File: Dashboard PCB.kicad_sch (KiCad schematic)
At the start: 36 parts, among them J1 Controls_Leader_Export_02x06, J2 Conn_02x03_CAN, J4 FAN_CTRL_01x02, J5 Horn_In_01x02, J6 Horn_Out_01x02, J7 Conn_02x03_CAN

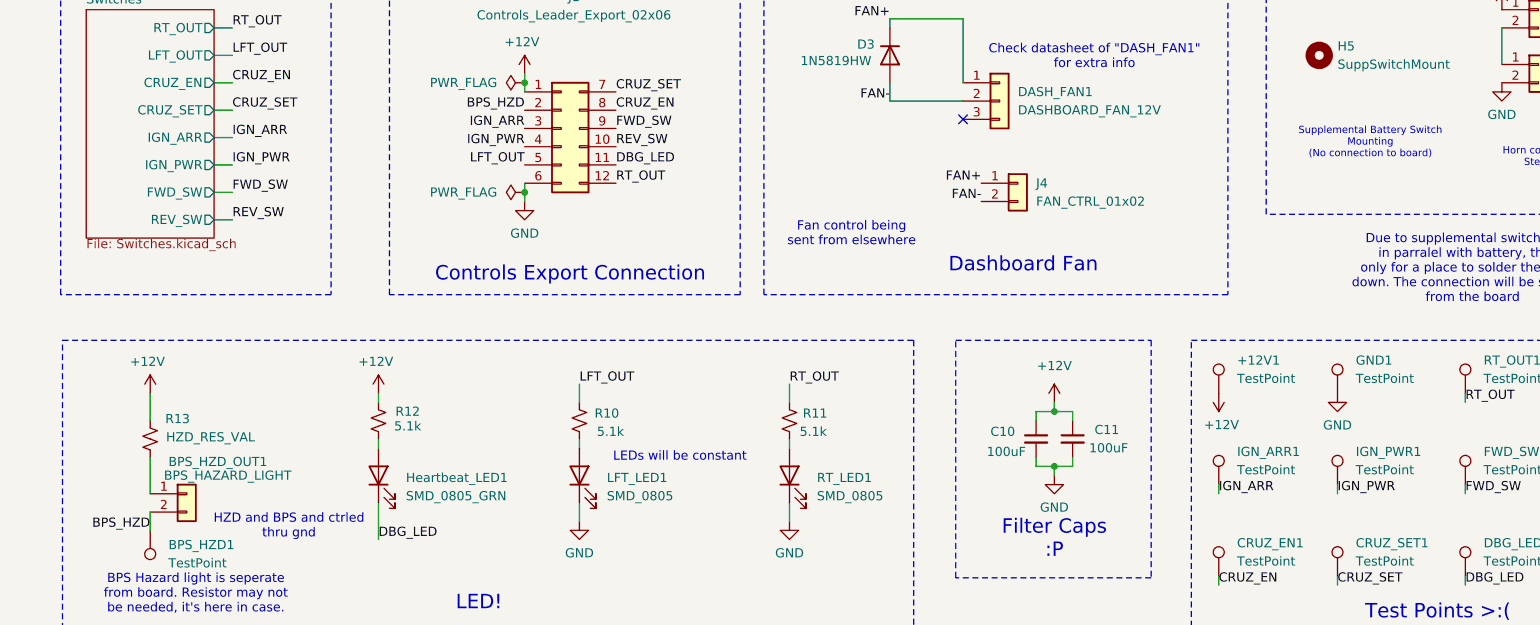
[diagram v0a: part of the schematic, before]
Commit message: Changed size and rerouted
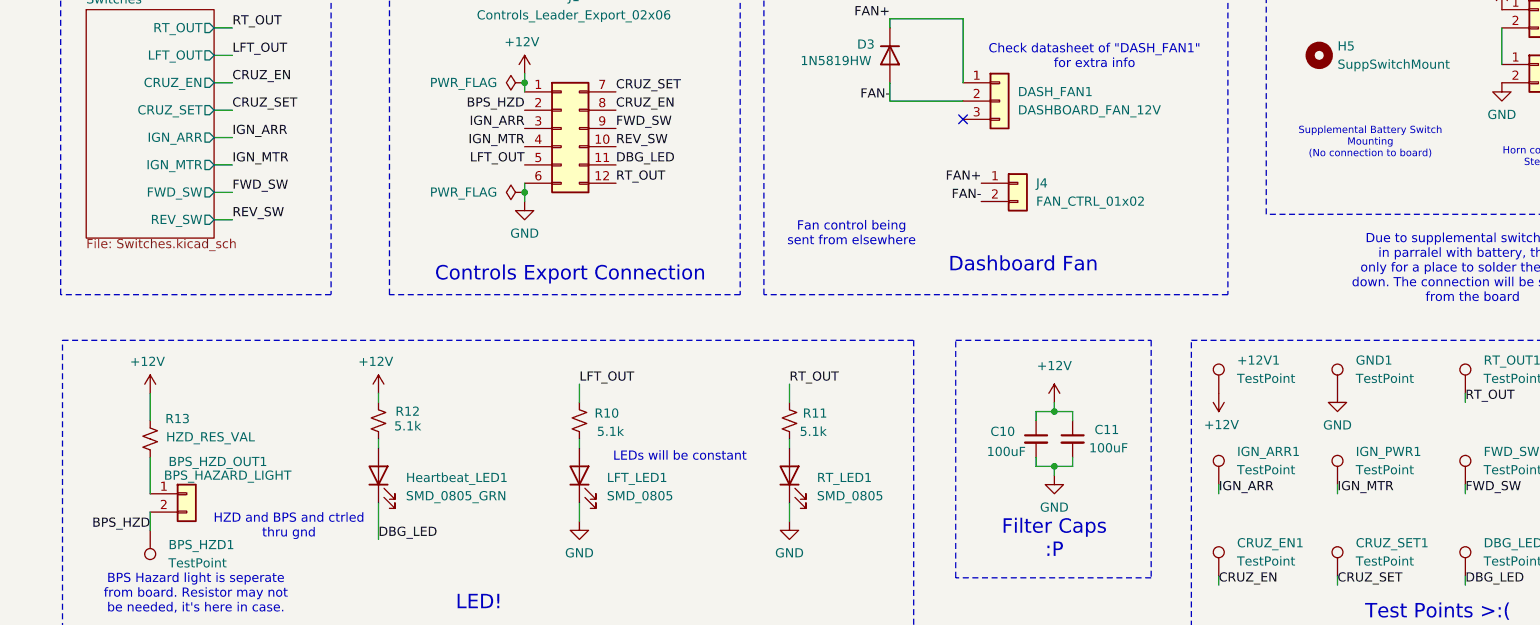
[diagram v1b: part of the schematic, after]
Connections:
- net IGN_PWR renamed IGN_MTR
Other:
- sheet Switches ports: added IGN_MTR; removed IGN_PWR
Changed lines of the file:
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@@
 		)
 	)
-	(label "IGN_PWR"
+	(label "IGN_MTR"
 		(at 95.25 87.63 180)
 		(fields_autoplaced yes)
@@
 		)
 	)
-	(label "IGN_PWR"
+	(label "IGN_MTR"
 		(at 54.61 90.17 0)
 		(fields_autoplaced yes)
@@
 		)
 	)
-	(label "IGN_PWR"
+	(label "IGN_MTR"
 		(at 208.28 135.89 0)
 		(fields_autoplaced yes)
@@
 			)
 		)
-		(pin "IGN_PWR" output
+		(pin "IGN_MTR" output
 			(at 52.07 90.17 0)
 			(effects

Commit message: A bunch of stuff
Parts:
- removed BPS_HZD_OUT1: BPS_HAZARD_LIGHT, Connector_Molex:Molex_Micro-Fit_3.0_43650-0215_1x02_P3.00mm_Vertical, symbol Connector_Generic:Conn_01x02
- added BPS_HZD_LED1: SMD_0805_RED, LED_SMD:LED_0805_2012Metric, symbol Device:LED
- added J8: Supp_Out, Connector_Molex:Molex_Micro-Fit_3.0_43650-0200_1x02_P3.00mm_Horizontal, symbol Connector_Generic:Conn_01x02
- added J9: Supp_In, Connector_Molex:Molex_Micro-Fit_3.0_43650-0215_1x02_P3.00mm_Vertical, symbol Connector_Generic:Conn_01x02
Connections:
- net BPS_HZD: now also BPS_HZD_LED1.1 (K)
- net at R13.2: now also BPS_HZD_LED1.2 (A)
- new net Supp+: J8.1 (Pin_1), J9.1 (Pin_1)
- new net Supp-: J8.2 (Pin_2), J9.2 (Pin_2)
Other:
- note removed: "BPS Hazard light is seperate from board. Resistor may not be needed, it's here in case."
- note removed: "HZD and BPS and ctrled thru gnd"
- note removed: "Supplemental Battery Switch Mounting (No connection to board)"
- moved on the sheet: H5

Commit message: Supp changes
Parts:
- added D4: LED, LED_SMD:LED_0805_2012Metric, symbol Device:LED
- added R14: 5.1k, Resistor_SMD:R_0805_2012Metric, symbol Device:R_Small_US
- J8: footprint Connector_Molex:Molex_Micro-Fit_3.0_43650-0200_1x02_P3.00mm_Horizontal -> Connector_Molex:Molex_Micro-Fit_3.0_43650-0300_1x03_P3.00mm_Horizontal; symbol Connector_Generic:Conn_01x02 -> Connector_Generic:Conn_01x03
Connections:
- net Supp-: now also J8.3 (Pin_3), D4.1 (K); no longer J8.2 (Pin_2), J9.2 (Pin_2)
- new net: D4.2 (A), R14.2
- new net LV_EN: J8.2 (Pin_2), J9.2 (Pin_2), R14.1
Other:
- moved on the sheet: H5, J9

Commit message: Final changes for now
added p/n n stuff
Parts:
- D3: P/N (none) -> 1N5819HW-7-F
- D4: P/N (none) -> APTD2012LCGCK
- DASH_FAN1, J8: P/N (none) -> 43650-0300
- J1: P/N (none) -> 43045-1200
- J2: P/N (none) -> 43045-0600
- J4, J5, J6: P/N (none) -> 43650-0200
- J7: P/N (none) -> 43045-0400
- J9: P/N (none) -> 43650-0215

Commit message: Uhh
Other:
- note added: "Might need to add mosfet between horn so there isnt a bunch of current going thru horn button"
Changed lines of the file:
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@@
+		)
+	)
+	(text "Might need to add mosfet between horn\nso there isnt a bunch of current going thru\nhorn button"
+		(exclude_from_sim no)
+		(at 279.146 77.216 0)
+		(effects
+			(font
+				(size 1.27 1.27)
+			)
 		)
 	)

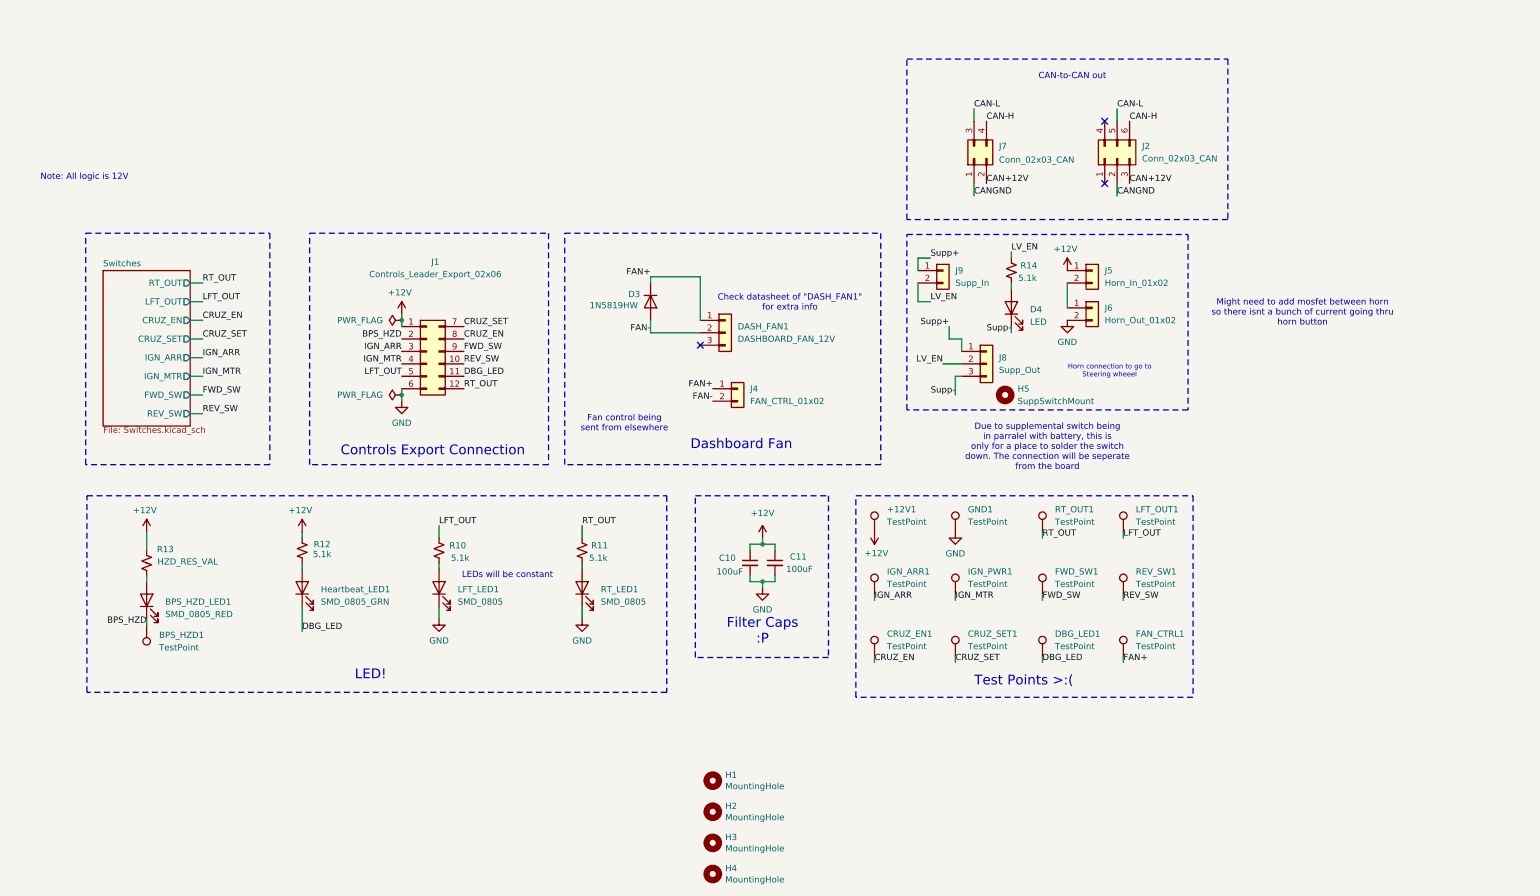
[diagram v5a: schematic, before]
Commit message: Delete submodule directory
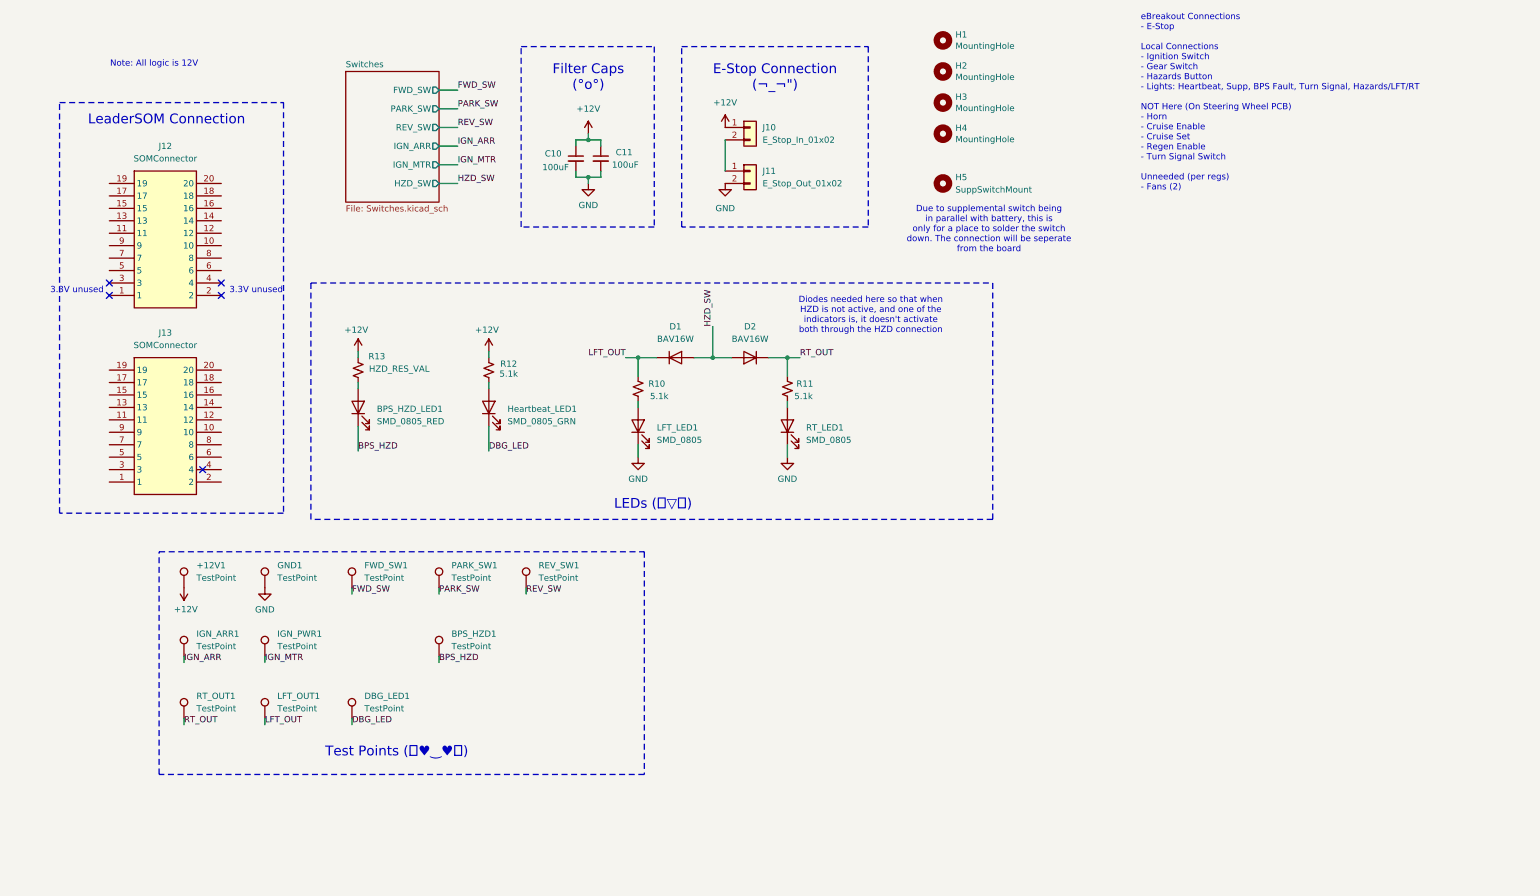
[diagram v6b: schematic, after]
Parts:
- removed CRUZ_EN1, CRUZ_SET1, FAN_CTRL1: TestPoint, TestPoint:TestPoint_Pad_1.0x1.0mm, symbol Connector:TestPoint
- removed D3: 1N5819HW, Diode_SMD:D_SOD-123, symbol Device:D
- removed D4: LED, LED_SMD:LED_0805_2012Metric, symbol Device:LED
- removed DASH_FAN1: DASHBOARD_FAN_12V, Connector_Molex:Molex_Micro-Fit_3.0_43650-0300_1x03_P3.00mm_Horizontal, symbol Connector_Generic:Conn_01x03
- removed J1: Controls_Leader_Export_02x06, Connector_Molex:Molex_Micro-Fit_3.0_43045-1200_2x06_P3.00mm_Horizontal, symbol Connector_Generic:Conn_02x06_Top_Bottom
- removed J2: Conn_02x03_CAN, Connector_Molex:Molex_Micro-Fit_3.0_43045-0600_2x03_P3.00mm_Horizontal, symbol Connector_Generic:Conn_02x03_Top_Bottom
- removed J4: FAN_CTRL_01x02, Connector_Molex:Molex_Micro-Fit_3.0_43650-0200_1x02_P3.00mm_Horizontal, symbol Connector_Generic:Conn_01x02
- removed J5: Horn_In_01x02, Connector_Molex:Molex_Micro-Fit_3.0_43650-0200_1x02_P3.00mm_Horizontal, symbol Connector_Generic:Conn_01x02
- removed J6: Horn_Out_01x02, Connector_Molex:Molex_Micro-Fit_3.0_43650-0200_1x02_P3.00mm_Horizontal, symbol Connector_Generic:Conn_01x02
- removed J7: Conn_02x03_CAN, Connector_Molex:Molex_Micro-Fit_3.0_43045-0400_2x02_P3.00mm_Horizontal, symbol Connector_Generic:Conn_02x02_Top_Bottom
- removed J8: Supp_Out, Connector_Molex:Molex_Micro-Fit_3.0_43650-0300_1x03_P3.00mm_Horizontal, symbol Connector_Generic:Conn_01x03
- removed J9: Supp_In, Connector_Molex:Molex_Micro-Fit_3.0_43650-0215_1x02_P3.00mm_Vertical, symbol Connector_Generic:Conn_01x02
- removed R14: 5.1k, Resistor_SMD:R_0805_2012Metric, symbol Device:R_Small_US
- added D1, D2: BAV16W, Diode_SMD:D_SOD-123, symbol Diode:BAV16W
- added J10: E_Stop_In_01x02, symbol Connector_Generic:Conn_01x02
- added J11: E_Stop_Out_01x02, symbol Connector_Generic:Conn_01x02
- added J12, J13: SOMConnector, UTSVT_Connectors:Molex_52465-2070, symbol connectors:SOMConnector
- added PARK_SW1: TestPoint, TestPoint:TestPoint_Pad_1.0x1.0mm, symbol Connector:TestPoint
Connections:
- net +12V: now also J10.1 (Pin_1)
- net GND: now also J11.2 (Pin_2)
- net LFT_OUT: now also D1.1 (K)
- net RT_OUT: now also D2.1 (K)
- new net: J10.2 (Pin_2), J11.1 (Pin_1)
- new net HZD_SW: D1.2 (A), D2.2 (A)
- new net PARK_SW: PARK_SW1.1
- no-connect marks 3 -> 5
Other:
- sheet Switches ports: added HZD_SW, PARK_SW; removed CRUZ_EN, CRUZ_SET, LFT_OUT, RT_OUT
- note added: "3.3V unused"
- note added: "Diodes needed here so that when HZD is not active, and one of the indicators is, it doesn't activate both through the HZD connection"
- note added: "Due to supplemental switch being in parallel with battery, this is only for a place to solder the switch down. The connection will be seperate from the board"
- note added: "E-Stop Connection (¬_¬")"
- note added: "Filter Caps (°o°)"
- note added: "LEDs (＾▽＾)"
- note added: "LeaderSOM Connection"
- note added: "Test Points (｡♥‿♥｡)"
- note added: "eBreakout Connections - E-Stop Local Connections - Ignition Switch - Gear Switch - Hazards Button - Lights: Heartbeat, Supp, BPS Fault, Turn Signal, Hazards/LFT/RT NOT Here (On Steering Wheel PCB) - Horn - Cruise Enable - Cruise Set - Regen Enable - Turn Signal Switch Unneeded (per regs) - Fans (2)"
- note removed: "CAN-to-CAN out"
- note removed: "Check datasheet of "DASH_FAN1" for extra info"
- note removed: "Controls Export Connection"
- note removed: "Dashboard Fan"
- note removed: "Due to supplemental switch being in parralel with battery, this is only for a place to solder the switch down. The connection will be seperate from the board"
- note removed: "Fan control being sent from elsewhere"
- note removed: "Filter Caps :P"
- note removed: "Horn connection to go to Steering wheeel"
- note removed: "LED!"
- note removed: "LEDs will be constant"
- note removed: "Might need to add mosfet between horn so there isnt a bunch of current going thru horn button"
- note removed: "Test Points >:("
- moved on the sheet: +12V1, BPS_HZD1, BPS_HZD_LED1, C10, C11, DBG_LED1, FWD_SW1, GND1, H1, H2, H3, H4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

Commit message: Schematic updates. Ready for review, I think.
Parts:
- removed J10: E_Stop_In_01x02, symbol Connector_Generic:Conn_01x02
- removed J11: E_Stop_Out_01x02, symbol Connector_Generic:Conn_01x02
- removed J12, J13: SOMConnector, UTSVT_Connectors:Molex_52465-2070, symbol connectors:SOMConnector
- added J1: ~, symbol connectors:LSOM_DaughterConn
- added J4: CarCAN_ConnIn_01x02, Connector_Molex:Molex_Micro-Fit_3.0_43650-0215_1x02_P3.00mm_Vertical, symbol Connector_Generic:Conn_01x02
- added J5: InternalCAN_ConnIn_01x02, Connector_Molex:Molex_Micro-Fit_3.0_43650-0215_1x02_P3.00mm_Vertical, symbol Connector_Generic:Conn_01x02
- added J6: InternalCAN_ConnOut_01x02, Connector_Molex:Molex_Micro-Fit_3.0_43650-0215_1x02_P3.00mm_Vertical, symbol Connector_Generic:Conn_01x02
- added J7: E_Stop_In_01x02, Connector_Molex:Molex_Micro-Fit_3.0_43650-0215_1x02_P3.00mm_Vertical, symbol Connector_Generic:Conn_01x02
- added J8: CarCAN_ConnOut_01x02, Connector_Molex:Molex_Micro-Fit_3.0_43650-0215_1x02_P3.00mm_Vertical, symbol Connector_Generic:Conn_01x02
- added J9: E_Stop_Out_01x02, Connector_Molex:Molex_Micro-Fit_3.0_43650-0215_1x02_P3.00mm_Vertical, symbol Connector_Generic:Conn_01x02
- BPS_HZD_LED1: P/N APTD2012LCGCK -> APTD2012LSURCK
- C10, C11: value 100uF -> 10uF; P/N C0805C103J5RACTU -> C0805C106M3PAC7210
- R10, R11, R12: value 5.1k -> 470; P/N CRCW0805100RFKEAHP -> CRCW0805470RFKEAC
- R13: value HZD_RES_VAL -> 470; P/N CRCW0805100RFKEAHP -> CRCW0805470RFKEAC
- renumbered +12V1 to +12V
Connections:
- net +12V: now also J1.21 (12VExt), J1.22 (12VExt), J1.23 (12VExt), J1.24 (12VExt), J7.1 (Pin_1); no longer R12.1, R13.1
- net FWD_SW: now also J1.20 (SPI2_SCK)
- net GND: now also BPS_HZD_LED1.1 (K), Heartbeat_LED1.1 (K), J1.10 (GND), J1.12 (GND), J1.13 (GND), J1.15 (GND), J1.25 (GND), J1.26 (GND), J1.27 (GND), J1.28 (GND), J1.29 (GND), J1.38 (GND), J1.40 (GND), J9.2 (Pin_2)
- net IGN_ARR: now also J1.44 (ADC1_IN3)
- net IGN_MTR: now also J1.42 (ADC1_IN2)
- net LFT_OUT: now also R11.1, J1.11 (I2C3_SCL); no longer R10.1
- net PARK_SW: now also J1.18 (SPI2_MOSI)
- net REV_SW: now also J1.16 (SPI2_CS)
- net RT_OUT: now also R12.1, J1.9 (I2C3_SDA); no longer R11.1
- net at RT_LED1.2 (A): now also R12.2; no longer R11.2
- net at Heartbeat_LED1.2 (A): now also R10.2; no longer R12.2
- net at LFT_LED1.2 (A): now also R11.2; no longer R10.2
- net BPS_HZD renamed BPS_HZD_OUT
- net BPS_HZD_OUT: now also R13.1, J1.19 (UART5_RX); no longer BPS_HZD_LED1.1 (K)
- net DBG_LED renamed DBG_LED_OUT
- net DBG_LED_OUT: now also R10.1, J1.17 (UART5_TX); no longer Heartbeat_LED1.1 (K)
- new net: J7.2 (Pin_2), J9.1 (Pin_1)
- new net +3.3V: J1.1 (+3.3V), J1.2 (+3.3V), J1.3 (+3.3V), J1.4 (+3.3V), J1.45 (+3.3V), J1.46 (+3.3V), J1.47 (+3.3V), J1.48 (+3.3V)
- new net CCAN_H: J1.30 (CCAN_H), J4.2 (Pin_2), J8.2 (Pin_2)
- new net CCAN_L: J1.32 (CCAN_L), J4.1 (Pin_1), J8.1 (Pin_1)
- new net ICAN_H: J1.6 (ICAN_H), J5.2 (Pin_2), J6.2 (Pin_2)
- new net ICAN_L: J1.8 (ICAN_L), J5.1 (Pin_1), J6.1 (Pin_1)
- no-connect marks 5 -> 12
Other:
- note added: "Breakout Connections - E-Stop Local Connections - Ignition Switch - Gear Switch - Hazards Button - Lights: Heartbeat, Supp, BPS Fault, Hazards+LFT/RT Turn Indicators - CAN: Internal CAN (Controls) & Car CAN (for things like BPS_FAULT, etc) NOT Here (On Steering Wheel PCB) - Horn - Cruise Enable - Cruise Set - Regen Enable - Turn Signal Switch (3-Pos Switch) Unneeded (per regs & cooling lead Kaden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"
- note added: "CAN Connections (｡♥‿♥｡)"
- note added: "Car CAN"
- note added: "Gear Switch"
- note added: "Ignition Switch"
- note added: "Internal/Controls CAN"
- note added: "Lights"
- note added: "Note: "_OUT" is appended to the end of signals that are output from the microcontroller"
- note added: "Notes: - All logic is 12V"
- note added: "Test Points (ノ◕ヮ◕)ノ*:・ﾟ✧"
- note removed: "3.3V unused"
- note removed: "Note: All logic is 12V"
- note removed: "Test Points (｡♥‿♥｡)"
- note removed: "eBreakout Connections - E-Stop Local Connections - Ignition Switch - Gear Switch - Hazards Button - Lights: Heartbeat, Supp, BPS Fault, Turn Signal, Hazards/LFT/RT NOT Here (On Steering Wheel PCB) - Horn - Cruise Enable - Cruise Set - Regen Enable - Turn Signal Switch Unneeded (per regs) - Fans (2)"
- moved on the sheet: +12V, BPS_HZD1, BPS_HZD_LED1, C10, C11, D1, D2, DBG_LED1, FWD_SW1, GND1, H1, H2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
